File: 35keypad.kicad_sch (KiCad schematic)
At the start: 104 parts, among them J1 USB_C_Receptacle_USB2.0, SW1 KEY_1_00, SW10 KEY_10_21, SW11 KEY_11_22, SW12 KEY_12_23, SW14 SW_SPST, SW15 SW_SPST, SW2 KEY_2_01, SW3 KEY_3_02, SW4 KEY_4_03, SW5 KEY_5_10, SW6 KEY_6_11, SW7 KEY_7_12, SW8 KEY_8_13, SW9 KEY_9_20, U1 RP2040, U2 NCP1117-3.3_SOT223, U3 W25Q128JVS, Y1 12MHz

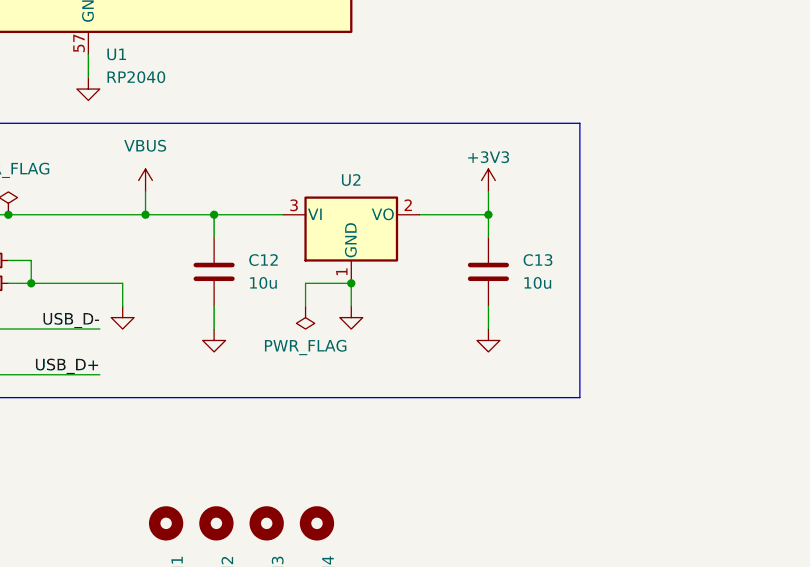
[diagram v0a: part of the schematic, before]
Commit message: schematic: edit some footprints
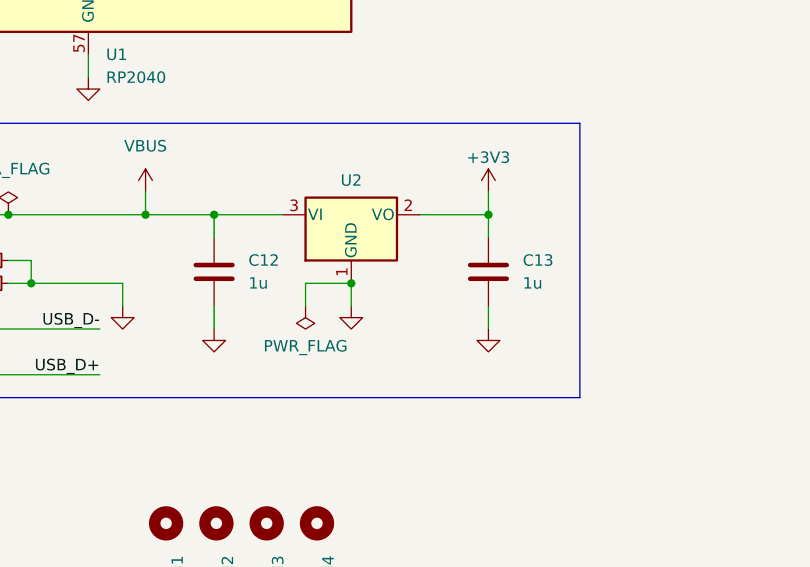
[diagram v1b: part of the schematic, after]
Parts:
- C12, C13: value 10u -> 1u; footprint Capacitor_SMD:C_0603_1608Metric -> Capacitor_SMD:C_0402_1005Metric
- D1, D10, D11, D12, D2, D3, D4, D5, D6, D7, D8, D9: footprint Diode_SMD:D_SOD-123 -> Diode_SMD:D_SOD-323
- U2: footprint Package_TO_SOT_SMD:SOT-223-3_TabPin2 -> Package_TO_SOT_SMD:SOT-23-3; JLCPCB_PART_NUMBER (none) -> C5446
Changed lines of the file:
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@@
 			)
 		)
-		(property "Footprint" "Diode_SMD:D_SOD-123"
+		(property "Footprint" "Diode_SMD:D_SOD-323"
 			(at 307.34 175.26 0)
 			(effects
@@
 			)
 		)
-		(property "Footprint" "Diode_SMD:D_SOD-123"
+		(property "Footprint" "Diode_SMD:D_SOD-323"
 			(at 254 83.82 0)
 			(effects
@@
 			)
 		)
-		(property "Footprint" "Diode_SMD:D_SOD-123"
+		(property "Footprint" "Diode_SMD:D_SOD-323"
 			(at 200.66 175.26 0)
 			(effects
@@
 			)
 		)
-		(property "Footprint" "Diode_SMD:D_SOD-123"
+		(property "Footprint" "Diode_SMD:D_SOD-323"
 			(at 365.76 106.68 0)
 			(effects
@@
 			)
 		)
-		(property "Footprint" "Diode_SMD:D_SOD-123"
+		(property "Footprint" "Diode_SMD:D_SOD-323"
 			(at 335.28 152.4 0)
 			(effects
@@
 			)
 		)
-		(property "Footprint" "Package_TO_SOT_SMD:SOT-223-3_TabPin2"
+		(property "Footprint" "Package_TO_SOT_SMD:SOT-23-3"
 			(at 106.68 160.02 0)
 			(effects
@@
 			)
 		)
+		(property "JLCPCB_PART_NUMBER" "C5446"
+			(at 106.68 165.1 0)
+			(effects
+				(font
+					(size 1.27 1.27)
+				)
+				(hide yes)
+			)
+		)
 		(pin "1"
 		)
@@
 			)
 		)
-		(property "Footprint" "Diode_SMD:D_SOD-123"
+		(property "Footprint" "Diode_SMD:D_SOD-323"
 			(at 335.28 106.68 0)
 			(effects
@@
 			)
 		)
-		(property "Footprint" "Diode_SMD:D_SOD-123"
+		(property "Footprint" "Diode_SMD:D_SOD-323"
 			(at 254 129.54 0)
 			(effects
@@
 			)
 		)
-		(property "Footprint" "Diode_SMD:D_SOD-123"
+		(property "Footprint" "Diode_SMD:D_SOD-323"
 			(at 279.4 129.54 0)
 			(effects
@@
 			)
 		)
-		(property "Footprint" "Diode_SMD:D_SOD-123"
+		(property "Footprint" "Diode_SMD:D_SOD-323"
 			(at 254 152.4 0)
 			(effects
@@
 			)
 		)
-		(property "Footprint" "Diode_SMD:D_SOD-123"
+		(property "Footprint" "Diode_SMD:D_SOD-323"
 			(at 226.06 83.82 0)
 			(effects
@@
 			)
 		)
-		(property "Footprint" "Diode_SMD:D_SOD-123"
+		(property "Footprint" "Diode_SMD:D_SOD-323"
 			(at 254 106.68 0)
 			(effects
@@
 			)
 		)
-		(property "Footprint" "Diode_SMD:D_SOD-123"
+		(property "Footprint" "Diode_SMD:D_SOD-323"
 			(at 307.34 83.82 0)
 			(effects
@@
 			)
 		)
-		(property "Footprint" "Diode_SMD:D_SOD-123"
+		(property "Footprint" "Diode_SMD:D_SOD-323"
 			(at 200.66 152.4 0)
 			(effects
@@
 			)
 		)
-		(property "Footprint" "Diode_SMD:D_SOD-123"
+		(property "Footprint" "Diode_SMD:D_SOD-323"
 			(at 279.4 106.68 0)
 			(effects
@@
 			)
 		)
-		(property "Footprint" "Diode_SMD:D_SOD-123"
+		(property "Footprint" "Diode_SMD:D_SOD-323"
 			(at 200.66 129.54 0)
 			(effects
@@
 			)
 		)
-		(property "Footprint" "Diode_SMD:D_SOD-123"
+		(property "Footprint" "Diode_SMD:D_SOD-323"
 			(at 335.28 83.82 0)
 			(effects
@@
 			)
 		)
-		(property "Value" "10u"
+		(property "Value" "1u"
 			(at 125.73 172.7199 0)
 			(effects
@@
 			)
 		)
-		(property "Footprint" "Capacitor_SMD:C_0603_1608Metric"
+		(property "Footprint" "Capacitor_SMD:C_0402_1005Metric"
 			(at 122.8852 175.26 0)
 			(effects
@@
 			)
 		)
-		(property "Footprint" "Diode_SMD:D_SOD-123"
+		(property "Footprint" "Diode_SMD:D_SOD-323"
 			(at 200.66 83.82 0)
 			(effects
@@
 			)
 		)
-		(property "Footprint" "Diode_SMD:D_SOD-123"
+		(property "Footprint" "Diode_SMD:D_SOD-323"
 			(at 254 175.26 0)
 			(effects
@@
 			)
 		)
-		(property "Footprint" "Diode_SMD:D_SOD-123"
+		(property "Footprint" "Diode_SMD:D_SOD-323"
 			(at 335.28 175.26 0)
 			(effects
@@
 			)
 		)
-		(property "Footprint" "Diode_SMD:D_SOD-123"
+		(property "Footprint" "Diode_SMD:D_SOD-323"
 			(at 365.76 129.54 0)
 			(effects
@@
 			)
 		)
-		(property "Footprint" "Diode_SMD:D_SOD-123"
+		(property "Footprint" "Diode_SMD:D_SOD-323"
 			(at 226.06 175.26 0)
 			(effects
@@
 			)
 		)
-		(property "Footprint" "Diode_SMD:D_SOD-123"
+		(property "Footprint" "Diode_SMD:D_SOD-323"
 			(at 226.06 129.54 0)
 			(effects
@@
 			)
 		)
-		(property "Footprint" "Diode_SMD:D_SOD-123"
+		(property "Footprint" "Diode_SMD:D_SOD-323"
 			(at 335.28 129.54 0)
 			(effects
@@
 			)
 		)
-		(property "Footprint" "Diode_SMD:D_SOD-123"
+		(property "Footprint" "Diode_SMD:D_SOD-323"
 			(at 307.34 129.54 0)
 			(effects
@@
 			)
 		)
-		(property "Footprint" "Diode_SMD:D_SOD-123"
+		(property "Footprint" "Diode_SMD:D_SOD-323"
 			(at 307.34 106.68 0)
 			(effects
@@
 			)
 		)
-		(property "Footprint" "Diode_SMD:D_SOD-123"
+		(property "Footprint" "Diode_SMD:D_SOD-323"
 			(at 365.76 152.4 0)
 			(effects
@@
 			)
 		)
-		(property "Footprint" "Diode_SMD:D_SOD-123"
+		(property "Footprint" "Diode_SMD:D_SOD-323"
 			(at 365.76 83.82 0)
 			(effects
@@
 			)
 		)
-		(property "Footprint" "Diode_SMD:D_SOD-123"
+		(property "Footprint" "Diode_SMD:D_SOD-323"
 			(at 307.34 152.4 0)
 			(effects
@@
 			)
 		)
-		(property "Footprint" "Diode_SMD:D_SOD-123"
+		(property "Footprint" "Diode_SMD:D_SOD-323"
 			(at 200.66 106.68 0)
 			(effects
@@
 			)
 		)
-		(property "Footprint" "Diode_SMD:D_SOD-123"
+		(property "Footprint" "Diode_SMD:D_SOD-323"
 			(at 226.06 152.4 0)
 			(effects
@@
 			)
 		)
-		(property "Footprint" "Diode_SMD:D_SOD-123"
+		(property "Footprint" "Diode_SMD:D_SOD-323"
 			(at 365.76 175.26 0)
 			(effects
@@
 			)
 		)
-		(property "Footprint" "Diode_SMD:D_SOD-123"
+		(property "Footprint" "Diode_SMD:D_SOD-323"
 			(at 279.4 175.26 0)
 			(effects
@@
 			)
 		)
-		(property "Footprint" "Diode_SMD:D_SOD-123"
+		(property "Footprint" "Diode_SMD:D_SOD-323"
 			(at 279.4 83.82 0)
 			(effects
@@
 			)
 		)
-		(property "Footprint" "Diode_SMD:D_SOD-123"
+		(property "Footprint" "Diode_SMD:D_SOD-323"
 			(at 226.06 106.68 0)
 			(effects
@@
 			)
 		)
-		(property "Value" "10u"
+		(property "Value" "1u"
 			(at 95.25 172.7199 0)
 			(effects
@@
 			)
 		)
-		(property "Footprint" "Capacitor_SMD:C_0603_1608Metric"
+		(property "Footprint" "Capacitor_SMD:C_0402_1005Metric"
 			(at 92.4052 175.26 0)
 			(effects
@@
 			)
 		)
-		(property "Footprint" "Diode_SMD:D_SOD-123"
+		(property "Footprint" "Diode_SMD:D_SOD-323"
 			(at 279.4 152.4 0)
 			(effects

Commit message: files: add finished pcb layout
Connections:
- net COL_0: now also U1.36 (GPIO24); no longer U1.35 (GPIO23)
- net COL_1: now also U1.35 (GPIO23); no longer U1.36 (GPIO24)
- net COL_2: now also U1.34 (GPIO22); no longer U1.15 (GPIO12)
- net COL_3: now also U1.13 (GPIO10); no longer U1.14 (GPIO11)
- net COL_4: now also U1.8 (GPIO6); no longer U1.13 (GPIO10)
- net COL_5: now also U1.5 (GPIO3); no longer U1.8 (GPIO6)
- net COL_6: now also U1.2 (GPIO0); no longer U1.7 (GPIO5)
- net ROW_1: now also U1.32 (GPIO21); no longer U1.34 (GPIO22)
- net ROW_3: now also U1.29 (GPIO18); no longer U1.17 (GPIO14)
- net ROW_4: now also U1.28 (GPIO17); no longer U1.16 (GPIO13)
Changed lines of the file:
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@@
 	)
 	(no_connect
-		(at 109.22 63.5)
+		(at 109.22 76.2)
 	)
 	(no_connect
@@
 	)
 	(no_connect
-		(at 109.22 109.22)
+		(at 109.22 96.52)
 	)
 	(no_connect
@@
 	)
 	(no_connect
+		(at 109.22 93.98)
+	)
+	(no_connect
 		(at 109.22 86.36)
 	)
@@
 	)
 	(no_connect
+		(at 109.22 99.06)
+	)
+	(no_connect
 		(at 109.22 73.66)
 	)
@@
 	)
 	(no_connect
-		(at 109.22 106.68)
-	)
-	(no_connect
 		(at 58.42 195.58)
 	)
@@
 	)
 	(no_connect
-		(at 109.22 116.84)
-	)
-	(no_connect
 		(at 109.22 134.62)
 	)
@@
 	)
 	(no_connect
-		(at 109.22 71.12)
+		(at 109.22 91.44)
 	)
 	(wire
@@
 	(wire
 		(pts
-			(xy 109.22 99.06) (xy 119.38 99.06)
+			(xy 109.22 109.22) (xy 119.38 109.22)
 		)
 		(stroke
@@
 	(wire
 		(pts
-			(xy 109.22 91.44) (xy 119.38 91.44)
+			(xy 109.22 88.9) (xy 119.38 88.9)
 		)
 		(stroke
@@
 	(wire
 		(pts
-			(xy 109.22 78.74) (xy 118.11 78.74)
+			(xy 109.22 71.12) (xy 118.11 71.12)
 		)
 		(stroke
@@
 	(wire
 		(pts
-			(xy 109.22 124.46) (xy 119.38 124.46)
+			(xy 109.22 121.92) (xy 119.38 121.92)
 		)
 		(stroke
@@
 	(wire
 		(pts
-			(xy 109.22 88.9) (xy 119.38 88.9)
+			(xy 109.22 78.74) (xy 119.38 78.74)
 		)
 		(stroke
@@
 	(wire
 		(pts
-			(xy 109.22 76.2) (xy 118.11 76.2)
+			(xy 109.22 63.5) (xy 118.11 63.5)
 		)
 		(stroke
@@
 	(wire
 		(pts
-			(xy 109.22 96.52) (xy 119.38 96.52)
+			(xy 109.22 106.68) (xy 119.38 106.68)
 		)
 		(stroke
@@
 	(wire
 		(pts
-			(xy 109.22 119.38) (xy 119.38 119.38)
+			(xy 109.22 116.84) (xy 119.38 116.84)
 		)
 		(stroke
@@
 	(wire
 		(pts
-			(xy 109.22 93.98) (xy 119.38 93.98)
+			(xy 109.22 119.38) (xy 119.38 119.38)
 		)
 		(stroke
@@
 	(wire
 		(pts
-			(xy 109.22 121.92) (xy 119.38 121.92)
+			(xy 109.22 124.46) (xy 119.38 124.46)
 		)
 		(stroke
@@
 	)
 	(label "COL_0"
-		(at 119.38 121.92 180)
+		(at 119.38 124.46 180)
 		(fields_autoplaced yes)
 		(effects
@@
 	)
 	(label "COL_2"
-		(at 119.38 93.98 180)
+		(at 119.38 119.38 180)
 		(fields_autoplaced yes)
 		(effects
@@
 	)
 	(label "ROW_3"
-		(at 119.38 99.06 180)
+		(at 119.38 109.22 180)
 		(fields_autoplaced yes)
 		(effects
@@
 	)
 	(label "ROW_1"
-		(at 119.38 119.38 180)
+		(at 119.38 116.84 180)
 		(fields_autoplaced yes)
 		(effects
@@
 	)
 	(label "COL_3"
-		(at 119.38 91.44 180)
+		(at 119.38 88.9 180)
 		(fields_autoplaced yes)
 		(effects
@@
 	)
 	(label "COL_6"
-		(at 118.11 76.2 180)
+		(at 118.11 63.5 180)
 		(fields_autoplaced yes)
 		(effects
@@
 	)
 	(label "COL_4"
-		(at 119.38 88.9 180)
+		(at 119.38 78.74 180)
 		(fields_autoplaced yes)
 		(effects
@@
 	)
 	(label "COL_1"
-		(at 119.38 124.46 180)
+		(at 119.38 121.92 180)
 		(fields_autoplaced yes)
 		(effects
@@
 	)
 	(label "COL_5"
-		(at 118.11 78.74 180)
+		(at 118.11 71.12 180)
 		(fields_autoplaced yes)
 		(effects
@@
 	)
 	(label "ROW_4"
-		(at 119.38 96.52 180)
+		(at 119.38 106.68 180)
 		(fields_autoplaced yes)
 		(effects
